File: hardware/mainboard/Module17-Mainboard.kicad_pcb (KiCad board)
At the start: 4 copper layers, 100 x 80 mm, 204 parts, among them IC301 LM4991MA, J301 CAT_TX, J302 CAT_RX, J401 Radio, J402 USB_C, J403 Radio_Opt, J404 Kenwood-3.5, J405 Kenwood-2.5, J406 2.54mm Header 7p, J407 KH-RJ45-58-8P8C, J408 STLink, J409 UART, J410 Speaker, J411 +12V, J412 Hirose FH12-26S-0.5SH(55), J413 Molex 532610271, Q201 MMBT3904, Q202 IRLML2244, Q301 IRLML2060, Q302 BSS138, Q303 BSS138, SW201 Tactile switch, SW202 Tactile switch, SW203 Tactile switch, SW204 Tactile switch, SW205 Tactile switch, SW206 Tactile switch, SW207 Tactile switch, SW208 Tactile switch, U201 STM32F405RGTx, U202 TPS7A2033, U203 TP6841S6, U301 MCP6002, U302 MAX9814, U401 USBLC6-2SC6, U501 MCP4551-103, U502 MCP4551-103, U503 MCP6002, U504 MCP6002, Y201 8 MHz

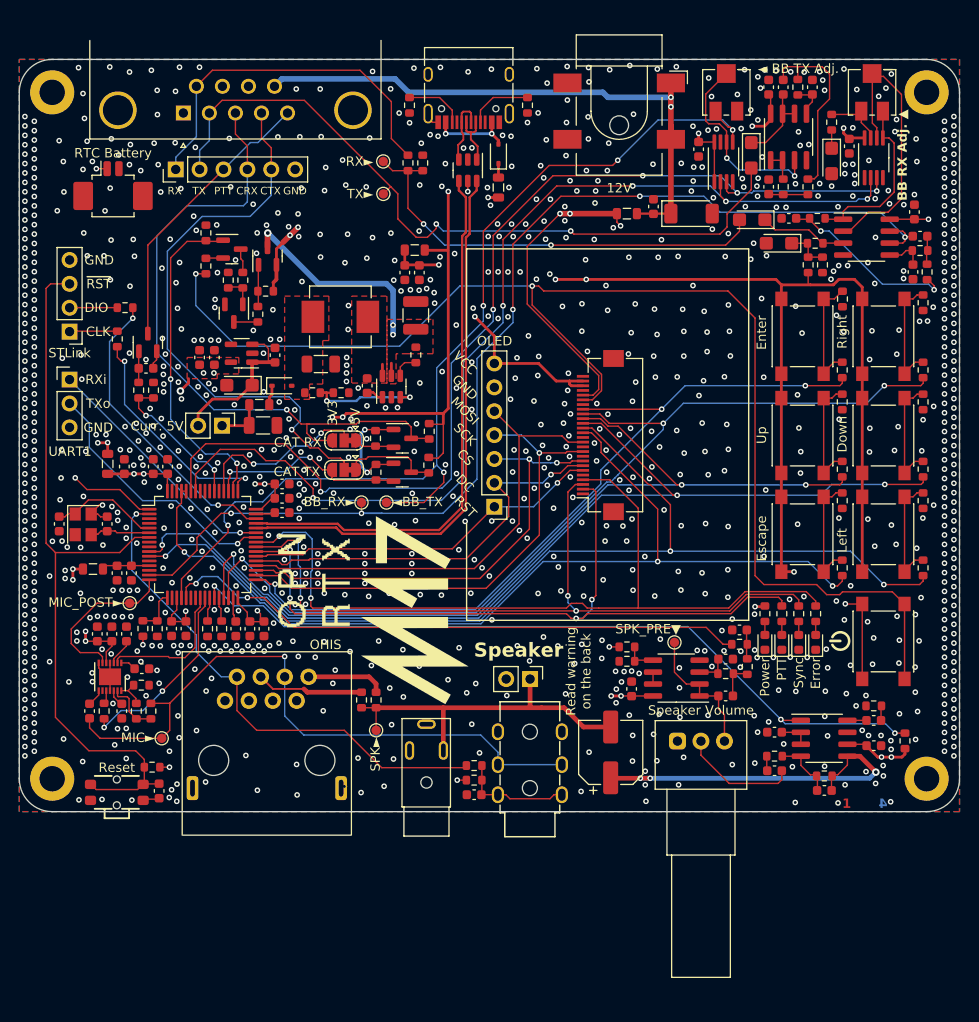
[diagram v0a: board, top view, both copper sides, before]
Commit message: Updated mainboard
Fixed dimension issues: moved some connectors closer to the edge of the board. Made the board 3.3mm longer.
Added pull-ups to the I2C bus.
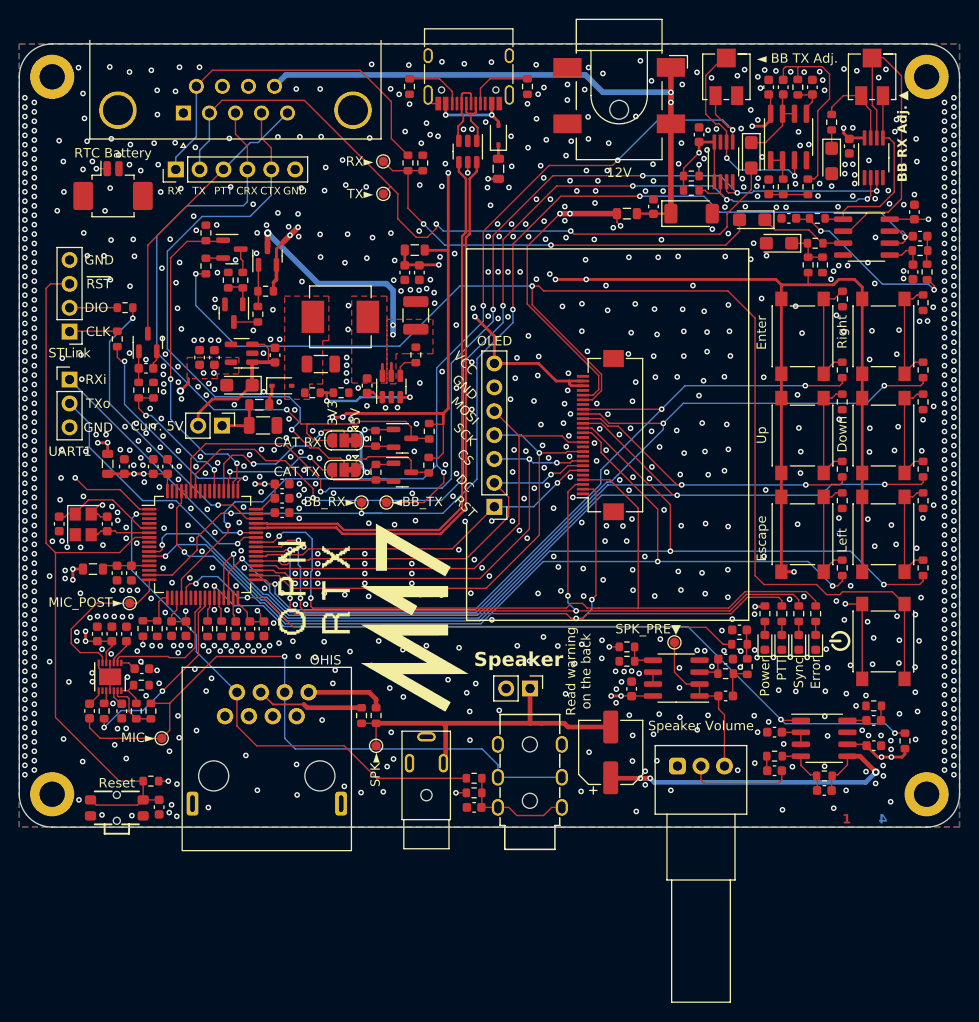
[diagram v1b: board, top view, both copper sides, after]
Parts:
- added R231: 2k2, Resistor_SMD:R_0603_1608Metric, F.Cu at (241.5, 60.9)
- added R232: 2k2, Resistor_SMD:R_0603_1608Metric, F.Cu at (241.5, 62.4)
- moved RV301 2.65 mm to (240.0, 123.7)
- moved D401 1.99 mm to (221.0, 56.5)
- moved FB401 1.99 mm to (221.0, 60.1)
- moved J402 1.99 mm to (217.8, 49.1)
- moved R401 1.99 mm to (224.1, 51.4)
- moved R402 1.99 mm to (211.5, 51.4)
- moved U401 1.99 mm to (217.7, 58.3)
- moved C215 1.73 mm to (184.9, 128.0)
- moved H103 1.65 mm to (173.5, 126.7)
- moved H104 1.65 mm to (266.5, 126.7)
- moved J407 1.65 mm to (196.3, 132.7)
- moved R409 1.65 mm to (207.9, 118.3)
- moved R410 1.65 mm to (206.4, 118.3)
- moved TP303 1.65 mm to (207.9, 121.5)
- moved H101 1.65 mm to (266.5, 50.4)
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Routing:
- net VDD: track 341.1 -> 349.5 mm
- net +5V: track 239.3 -> 243.3 mm
- net /Baseband/BB_RX_W: track 29.4 -> 33.3 mm
- net /Baseband/BB_RX_B: track 5.86 -> 9.33 mm
- net Net-(U301A--): track 14.9 -> 17.5 mm
- net I2C_SDA: track 110.8 -> 113.2 mm, vias 5 -> 6
- net I2C_SCL: track 109.0 -> 111.2 mm
- net USB_DN: track 59.0 -> 61.2 mm
- net USB_DP: track 58.4 -> 60.5 mm
- net MIC: track 68.2 -> 70.2 mm
- net /Baseband/BB_RX_A: track 18.3 -> 20.2 mm
- net GND: track 13.7 -> 11.9 mm, vias 1064 -> 1084
- net BASEBAND_TX: track 107.6 -> 109.2 mm
- net /Baseband/BB_TX_W: track 21.2 -> 22.8 mm
- net /Connectors/xUDN: track 7.48 -> 6.22 mm
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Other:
- board size 100 x 80 mm -> 100 x 83.3 mm
- board text added: "100.0000 mm x 83.3000 mm"
- board text added: "Revision 0.99b 12.2023"
- board text removed: "99.5000 mm x 80.0000 mm"
- board text removed: "Revision 0.99 12.2023"
- board text removed: "Volume knob sticks out of the board by : 1.6mm (PCB thickness for enclosure) + 2mm (nut thickness) + 0.5mm (washer thickness) + 0.4mm (tolerance margin) = 4.5mm"

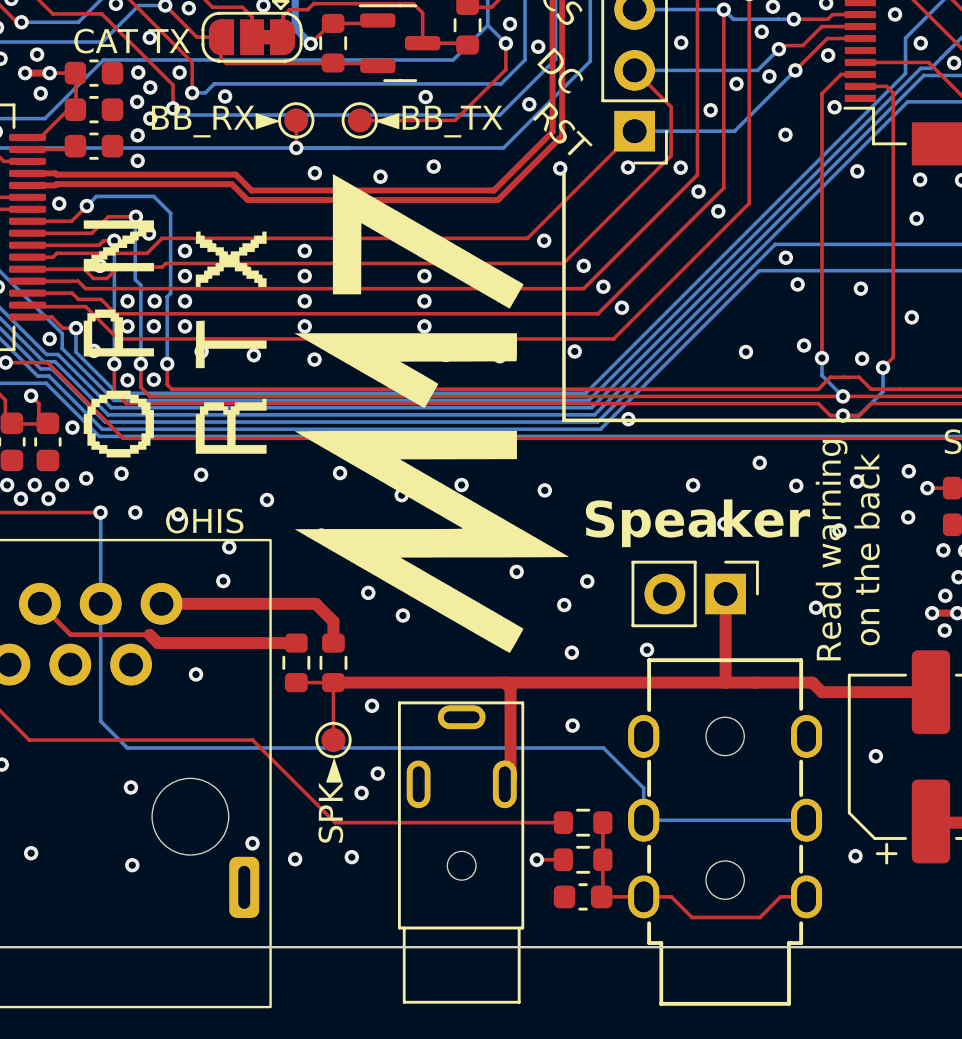
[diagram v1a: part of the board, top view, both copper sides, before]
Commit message: Updated mainboard
Replaced OHIS speaker resistors with larger 100 ohms resistors
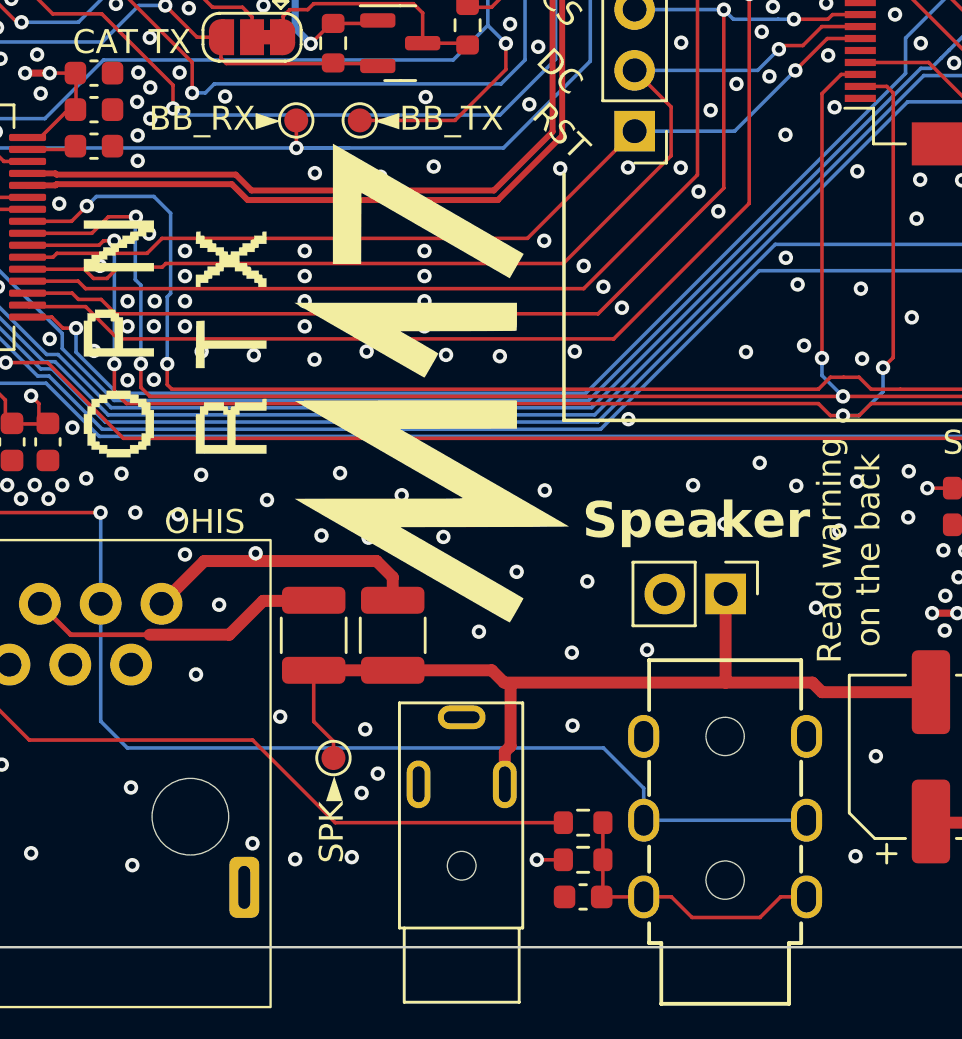
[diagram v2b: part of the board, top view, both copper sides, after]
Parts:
- R409, R410: value 0 -> 100; footprint Resistor_SMD:R_0603_1608Metric -> Resistor_SMD:R_1210_3225Metric
- moved R409 2.73 mm to (210.4, 117.1)
- moved R410 1.36 mm to (207.1, 117.1)
- moved LOGO101 1.27 mm to (212.1, 106.6)
- moved TP303 0.75 mm to (207.9, 122.2)
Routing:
- net Net-(J407-Pad8): track 8.88 -> 12.1 mm
- net SPEAKER: track 36.7 -> 37.7 mm
- net Net-(J407-Pad4): track 11.4 -> 12.3 mm
